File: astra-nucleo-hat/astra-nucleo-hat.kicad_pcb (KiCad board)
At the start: 4 copper layers, 58 x 82 mm, 47 parts, among them IC1 579-ATA6561-GAQW-N, IC2 74HC14PW,118, IC3 AT25EU0011A-SSHN-B, J1 PWR_CONN, J10 LED2_CONN, J11 DSP_CONN, J2 RPI_CONN, J3 CAN_CONN, J4 PWR_SIG_CONN, J5 I2C2_CONN, J6 BAT_CONN, J7 CAR_SIG_CONN, J8 JST_03, J9 LED1_CONN, Q1 IRLML6344, U3 MC3419, U5 LED1642GWPTR

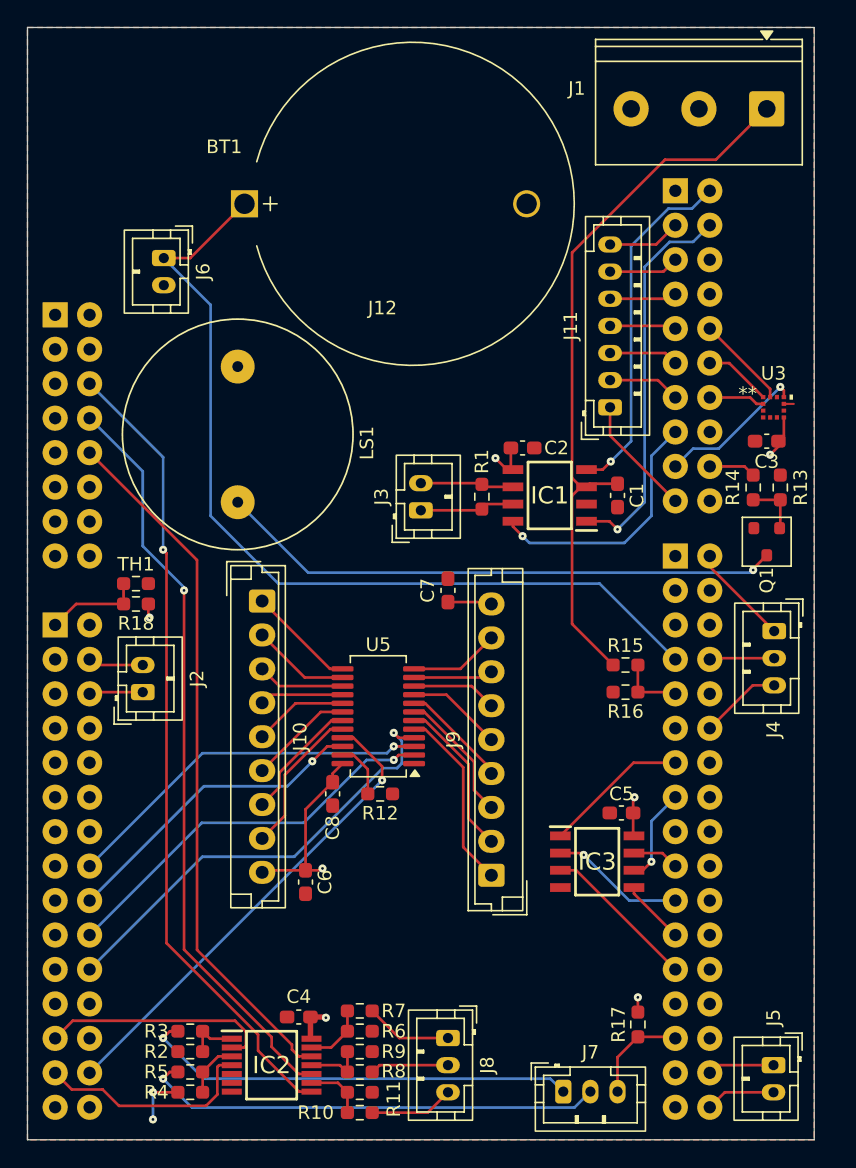
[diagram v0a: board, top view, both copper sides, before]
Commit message: HAT stitching and authored
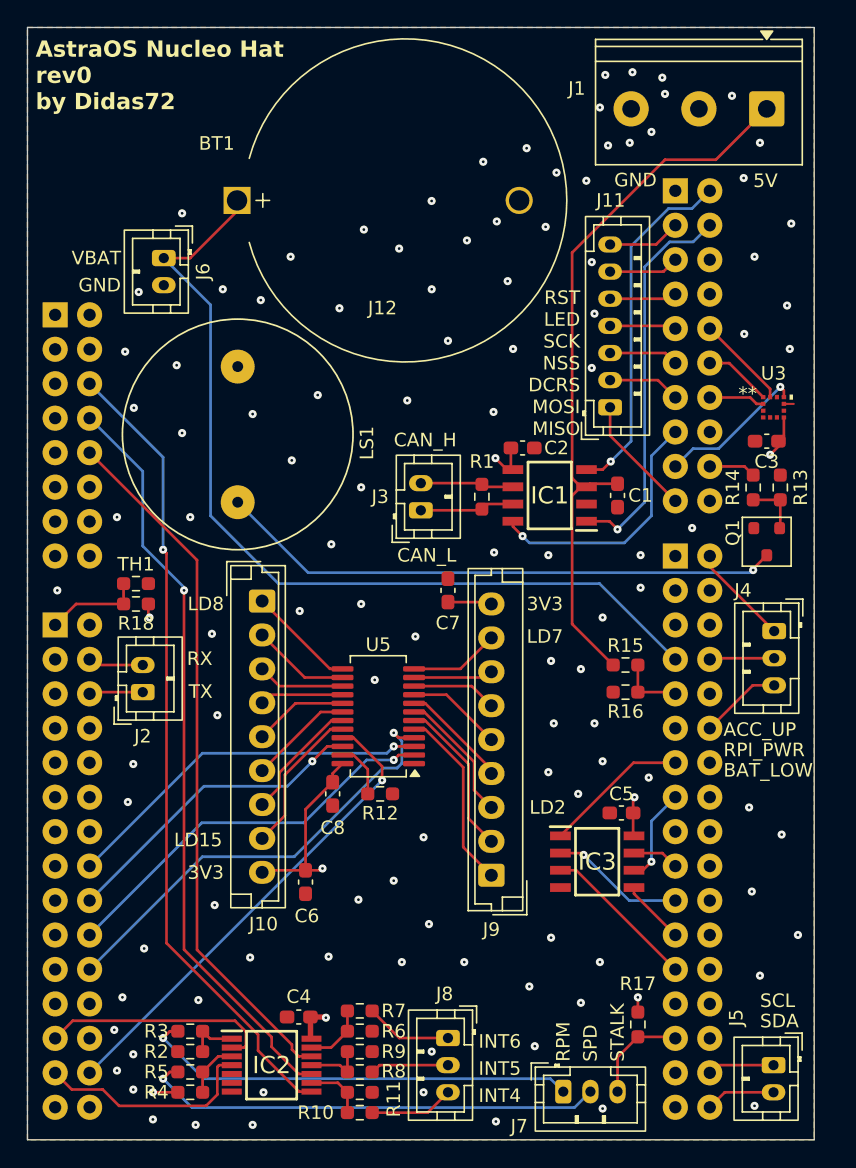
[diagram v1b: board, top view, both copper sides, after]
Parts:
- moved BT1 0.60 mm to (90.5, 53.2)
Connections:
- net I2C2_SDL renamed I2C2_SDA
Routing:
- net GND: track 4.58 -> 2.58 mm, vias 2 -> 111
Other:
- board text added: "3V3"
- board text added: "5V"
- board text added: "ACC_UP"
- board text added: "AstraOS Nucleo Hat rev0 by Didas72"
- board text added: "BAT_LOW"
- board text added: "CAN_H"
- board text added: "CAN_L"
- board text added: "GND"
- board text added: "INT4"
- board text added: "INT5"
- board text added: "INT6"
- board text added: "LD15"
- board text added: "LD2"
- board text added: "LD7"
- board text added: "LD8"
- board text added: "RPI_PWR"
- board text added: "RPM"
- board text added: "RST LED SCK NSS DCRS MOSI MISO"
- board text added: "RX"
- board text added: "SCL"
- board text added: "SDA"
- board text added: "SPD"
- board text added: "STALK"
- board text added: "TX"
- board text added: "VBAT"

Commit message: HAT decorated
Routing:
- net GND: vias 111 -> 110
- net +3V3: vias 7 -> 8

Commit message: HAT and ICP production files
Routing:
- net GND: vias 110 -> 109
- net +3V3: vias 8 -> 9
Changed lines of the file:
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@@
-	)
-	(via
-		(at 104.8 116)
-		(size 0.6)
-		(drill 0.2)
-		(layers "F.Cu" "B.Cu")
-		(net "GND")
 	)
 	(via
@@
 		(size 0.6)
 		(drill 0.2)
+		(layers "F.Cu" "B.Cu")
+		(net "+3V3")
+	)
+	(via
+		(at 104.8 116)
+		(size 0.6)
+		(drill 0.2)

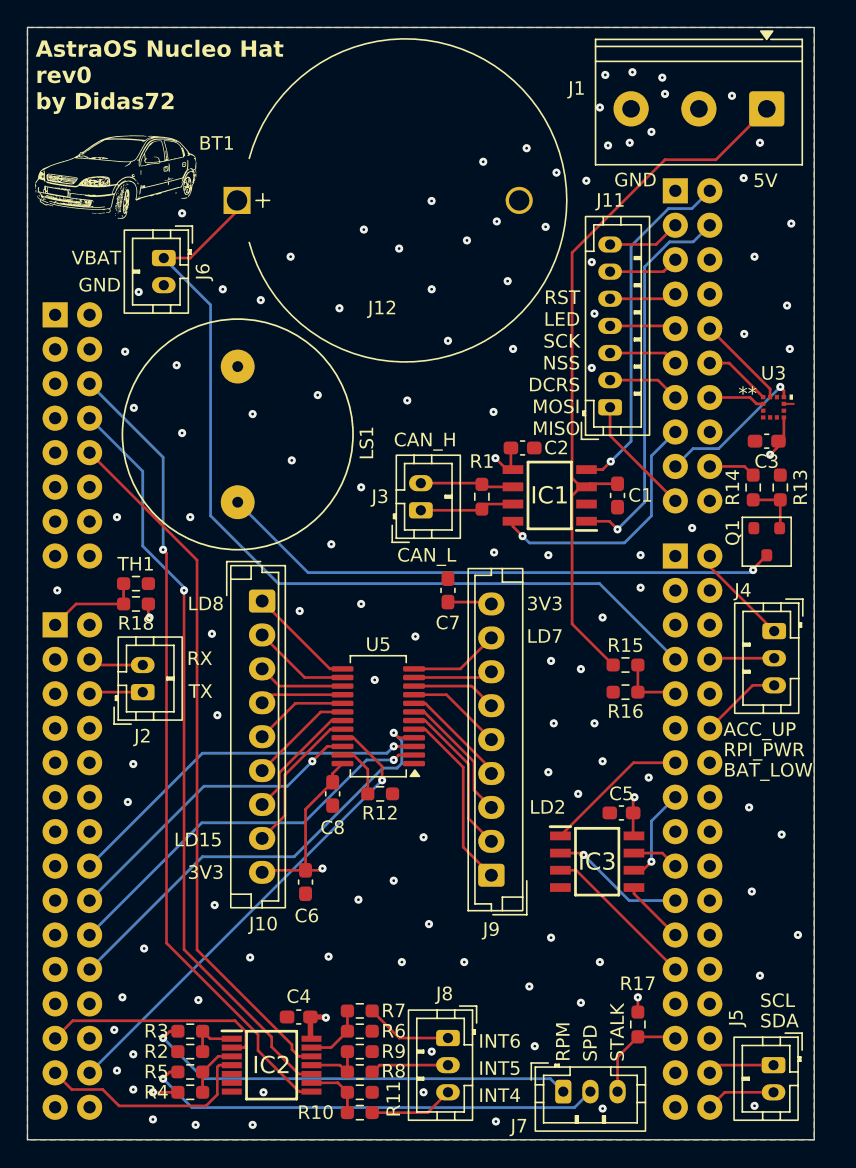
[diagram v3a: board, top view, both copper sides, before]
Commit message: Corrected 7 and 9 pin connectors in HAT
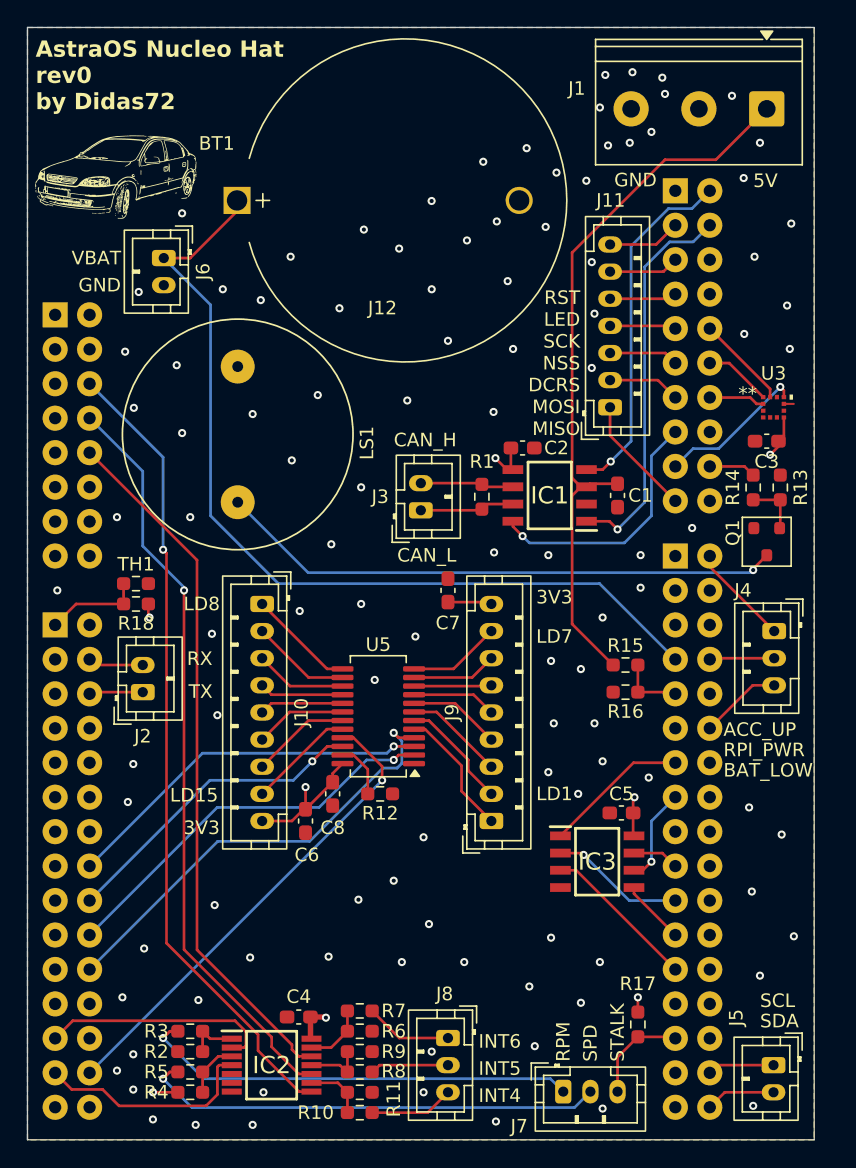
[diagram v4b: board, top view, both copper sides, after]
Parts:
- J10, J9: footprint Connector_JST:JST_EH_B9B-EH-A_1x09_P2.50mm_Vertical -> Connector_JST:JST_PH_B9B-PH-K_1x09_P2.00mm_Vertical
- R14: value 100 -> 120
- moved C6 4.50 mm to (95.5, 99.0)
- moved J9 4.00 mm to (109.2, 99.0)
- moved J10 0.22 mm to (92.3, 83.0)
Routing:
- net +3V3: track 31.5 -> 27.4 mm, vias 9 -> 10
- net LD0: track 13.6 -> 9.61 mm
- net LD1: track 11.7 -> 8.41 mm
- net LD15: track 11.0 -> 7.90 mm
- net LD2: track 9.84 -> 7.67 mm
- net LD14: track 9.12 -> 7.34 mm
- net LD3: track 8.02 -> 6.81 mm
- net LD13: track 7.72 -> 6.77 mm
- net LD4: track 7.07 -> 6.24 mm
- net LD12: track 6.94 -> 6.20 mm
- net LD5: track 6.30 -> 5.72 mm
- net GND: vias 109 -> 107
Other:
- board text added: "LD1"
- board text removed: "LD2"

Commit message: Changed HAT battery holder
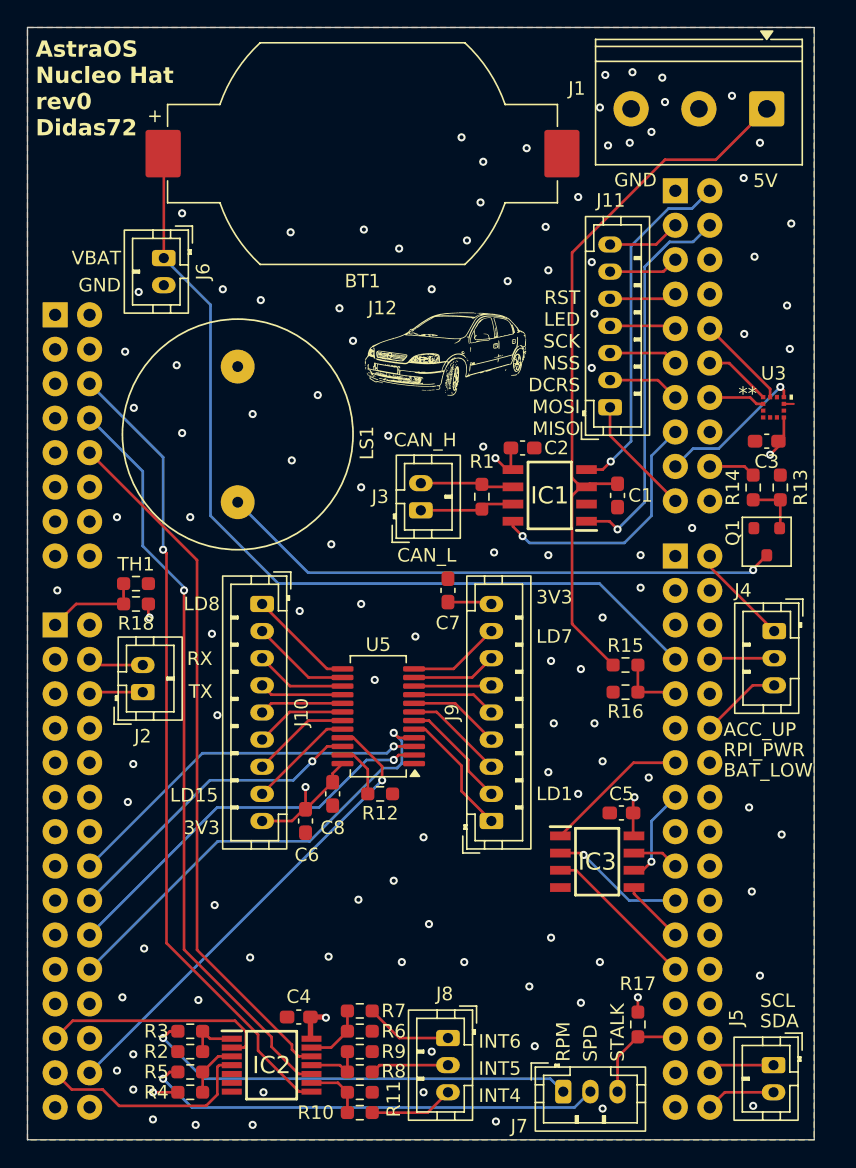
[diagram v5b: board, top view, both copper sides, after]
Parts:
- BT1: footprint Battery:BatteryHolder_MYOUNG_BS-07-A1BJ001_CR2032 -> Battery:BatteryHolder_Renata_SMTU2032-LF_1x2032
- moved BT1 9.87 mm to (99.7, 49.8)
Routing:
- net VBAT: track 67.5 -> 66.8 mm
- net GND: vias 107 -> 108
- net +3V3: vias 10 -> 7
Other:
- board text added: "AstraOS Nucleo Hat rev0 Didas72"
- board text removed: "AstraOS Nucleo Hat rev0 by Didas72"
